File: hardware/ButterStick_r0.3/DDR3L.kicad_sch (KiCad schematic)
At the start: 2 parts, among them U4 MT41K64M16TW-107_J-TR

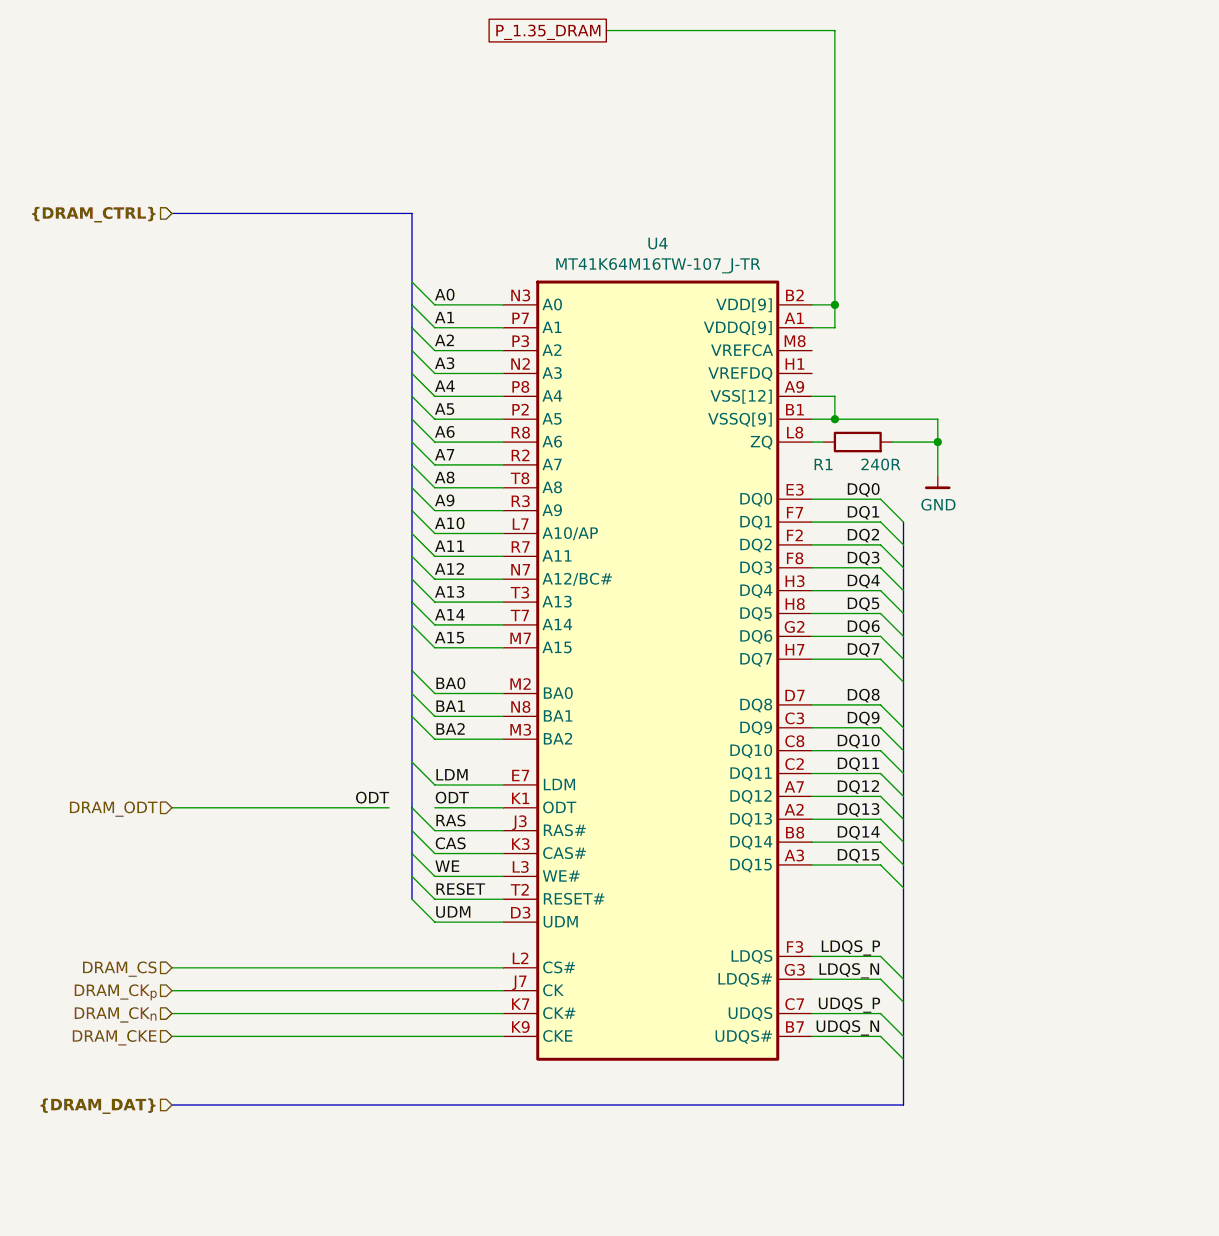
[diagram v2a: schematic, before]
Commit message: hw.r0_3: Inital routing of DDR3 done
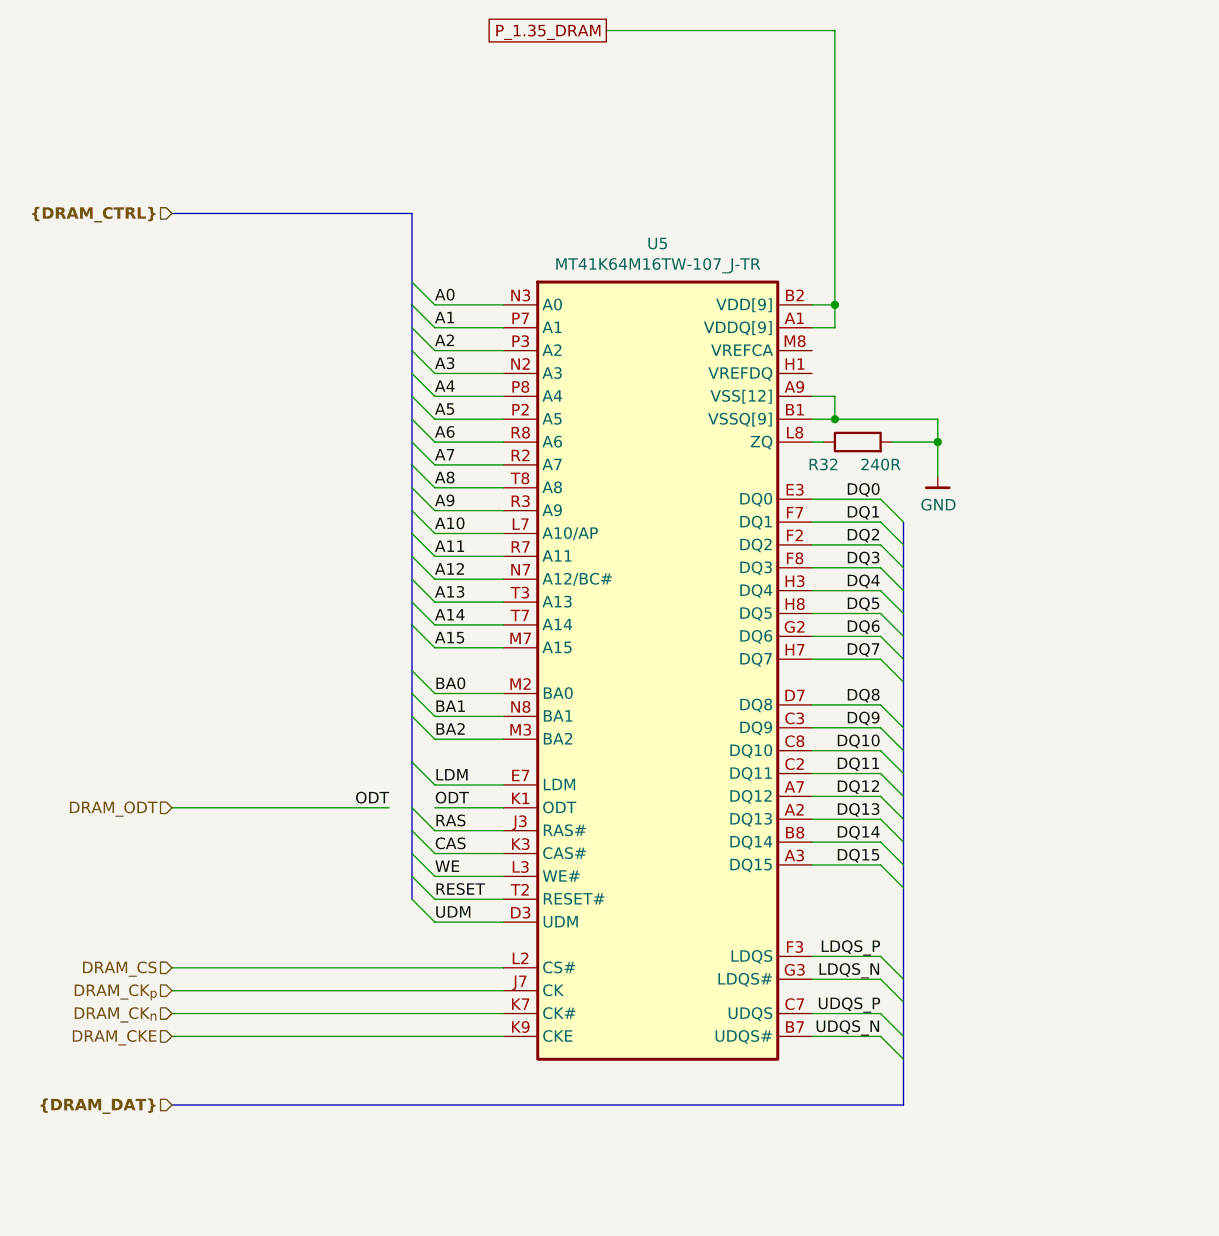
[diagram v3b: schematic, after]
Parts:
- renumbered R1 to R32, U4 to U5
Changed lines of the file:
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@@
 (kicad_sch (version 20200512) (host eeschema "5.99.0-unknown-711fc99~101~ubuntu18.04.1")
-  (page 1 20)
+  (page 14 20)
   (paper "A4")
   (junction (at 157.48 66.04))
@@
   (bus (pts (xy 83.82 154.94) (xy 165.1 154.94)))
   (bus (pts (xy 110.49 55.88) (xy 110.49 66.04)))
-  (bus (pts (xy 110.49 66.04) (xy 110.49 68.58)))
-  (bus (pts (xy 110.49 68.58) (xy 110.49 73.66)))
-  (bus (pts (xy 110.49 73.66) (xy 110.49 78.74)))
+  (bus (pts (xy 110.49 66.04) (xy 110.49 71.12)))
+  (bus (pts (xy 110.49 71.12) (xy 110.49 76.2)))
+  (bus (pts (xy 110.49 76.2) (xy 110.49 78.74)))
   (bus (pts (xy 110.49 78.74) (xy 110.49 83.82)))
   (bus (pts (xy 110.49 83.82) (xy 110.49 88.9)))
-  (bus (pts (xy 110.49 88.9) (xy 110.49 93.98)))
-  (bus (pts (xy 110.49 93.98) (xy 110.49 99.06)))
-  (bus (pts (xy 110.49 99.06) (xy 110.49 106.68)))
-  (bus (pts (xy 110.49 106.68) (xy 110.49 111.76)))
-  (bus (pts (xy 110.49 111.76) (xy 110.49 121.92)))
-  (bus (pts (xy 110.49 121.92) (xy 110.49 127)))
+  (bus (pts (xy 110.49 88.9) (xy 110.49 91.44)))
+  (bus (pts (xy 110.49 91.44) (xy 110.49 96.52)))
+  (bus (pts (xy 110.49 96.52) (xy 110.49 101.6)))
+  (bus (pts (xy 110.49 101.6) (xy 110.49 109.22)))
+  (bus (pts (xy 110.49 109.22) (xy 110.49 116.84)))
+  (bus (pts (xy 110.49 116.84) (xy 110.49 124.46)))
+  (bus (pts (xy 110.49 124.46) (xy 110.49 127)))
   (bus (pts (xy 110.49 127) (xy 110.49 132.08)))
   (bus (pts (xy 165.1 90.17) (xy 165.1 95.25)))
@@
   )
   (symbol (lib_id "Device:R") (at 160.02 81.28 90)
-    (property "Reference" "R1" (id 0) (at 156.21 83.82 90))
+    (property "Reference" "R32" (id 0) (at 156.21 83.82 90))
     (property "Value" "240R" (id 1) (at 162.56 83.82 90))
     (property "Footprint" "" (id 2) (at 160.02 83.058 90)
@@
   )
   (symbol (lib_id "gkl_mem:MT41K512M16TW") (at 137.16 96.52 0)
-    (property "Reference" "U4" (id 0) (at 137.795 59.2582 0))
+    (property "Reference" "U5" (id 0) (at 137.795 59.2582 0))
     (property "Value" "MT41K64M16TW-107_J-TR" (id 1) (at 137.795 61.5442 0))
     (property "Footprint" "Package_BGA:BGA-96_9.0x13.0mm_Layout2x3x16_P0.8mm" (id 2) (at 138.43 58.42 0)

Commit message: hw.r0_3: routed SYZYGY, begin routing RGMII/ULPI
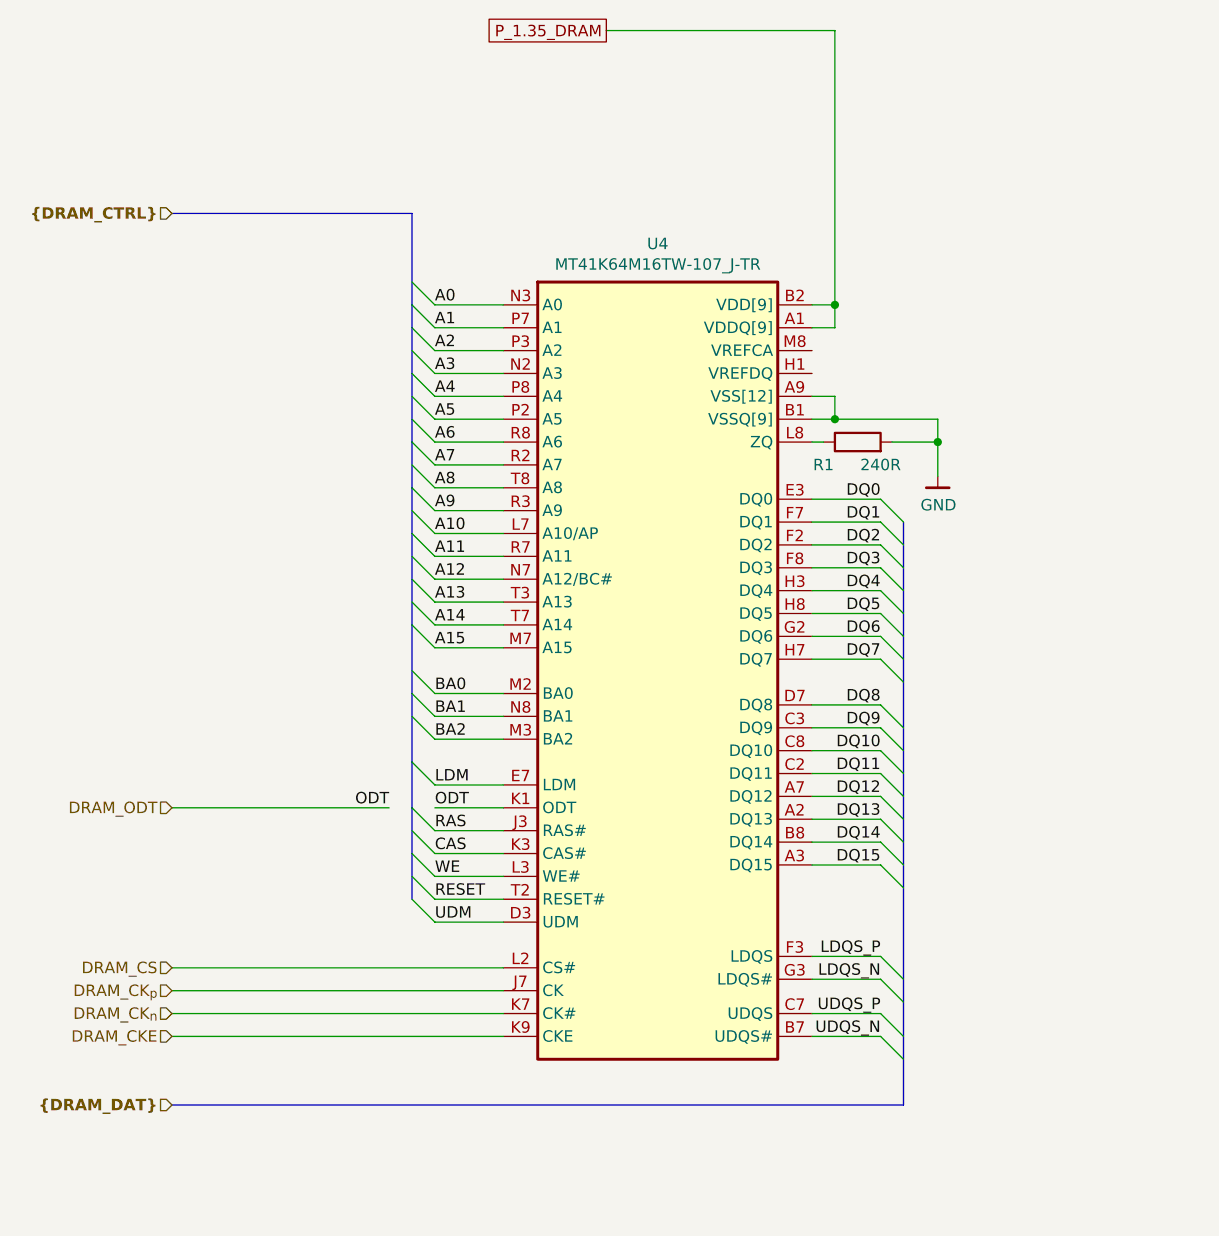
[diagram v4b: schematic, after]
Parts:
- renumbered R32 to R1, U5 to U4
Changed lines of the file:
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@@
 (kicad_sch (version 20200512) (host eeschema "5.99.0-unknown-711fc99~101~ubuntu18.04.1")
-  (page 14 20)
+  (page 1 19)
   (paper "A4")
   (junction (at 157.48 66.04))
@@
   (bus (pts (xy 83.82 154.94) (xy 165.1 154.94)))
   (bus (pts (xy 110.49 55.88) (xy 110.49 66.04)))
-  (bus (pts (xy 110.49 66.04) (xy 110.49 71.12)))
-  (bus (pts (xy 110.49 71.12) (xy 110.49 76.2)))
-  (bus (pts (xy 110.49 76.2) (xy 110.49 78.74)))
-  (bus (pts (xy 110.49 78.74) (xy 110.49 83.82)))
-  (bus (pts (xy 110.49 83.82) (xy 110.49 88.9)))
-  (bus (pts (xy 110.49 88.9) (xy 110.49 91.44)))
+  (bus (pts (xy 110.49 66.04) (xy 110.49 68.58)))
+  (bus (pts (xy 110.49 68.58) (xy 110.49 73.66)))
+  (bus (pts (xy 110.49 73.66) (xy 110.49 78.74)))
+  (bus (pts (xy 110.49 78.74) (xy 110.49 81.28)))
+  (bus (pts (xy 110.49 81.28) (xy 110.49 86.36)))
+  (bus (pts (xy 110.49 86.36) (xy 110.49 91.44)))
   (bus (pts (xy 110.49 91.44) (xy 110.49 96.52)))
   (bus (pts (xy 110.49 96.52) (xy 110.49 101.6)))
   (bus (pts (xy 110.49 101.6) (xy 110.49 109.22)))
   (bus (pts (xy 110.49 109.22) (xy 110.49 116.84)))
-  (bus (pts (xy 110.49 116.84) (xy 110.49 124.46)))
-  (bus (pts (xy 110.49 124.46) (xy 110.49 127)))
+  (bus (pts (xy 110.49 116.84) (xy 110.49 121.92)))
+  (bus (pts (xy 110.49 121.92) (xy 110.49 127)))
   (bus (pts (xy 110.49 127) (xy 110.49 132.08)))
   (bus (pts (xy 165.1 90.17) (xy 165.1 95.25)))
@@
   (bus (pts (xy 165.1 115.57) (xy 165.1 120.65)))
   (bus (pts (xy 165.1 120.65) (xy 165.1 125.73)))
-  (bus (pts (xy 165.1 125.73) (xy 165.1 130.81)))
-  (bus (pts (xy 165.1 130.81) (xy 165.1 143.51)))
+  (bus (pts (xy 165.1 125.73) (xy 165.1 128.27)))
+  (bus (pts (xy 165.1 128.27) (xy 165.1 140.97)))
+  (bus (pts (xy 165.1 140.97) (xy 165.1 143.51)))
   (bus (pts (xy 165.1 143.51) (xy 165.1 149.86)))
   (bus (pts (xy 165.1 149.86) (xy 165.1 154.94)))
@@
   )
   (symbol (lib_id "Device:R") (at 160.02 81.28 90)
-    (property "Reference" "R32" (id 0) (at 156.21 83.82 90))
+    (property "Reference" "R1" (id 0) (at 156.21 83.82 90))
     (property "Value" "240R" (id 1) (at 162.56 83.82 90))
     (property "Footprint" "" (id 2) (at 160.02 83.058 90)
@@
   )
   (symbol (lib_id "gkl_mem:MT41K512M16TW") (at 137.16 96.52 0)
-    (property "Reference" "U5" (id 0) (at 137.795 59.2582 0))
+    (property "Reference" "U4" (id 0) (at 137.795 59.2582 0))
     (property "Value" "MT41K64M16TW-107_J-TR" (id 1) (at 137.795 61.5442 0))
     (property "Footprint" "Package_BGA:BGA-96_9.0x13.0mm_Layout2x3x16_P0.8mm" (id 2) (at 138.43 58.42 0)

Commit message: hw.r0_3: major blocks roughly routed
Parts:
- renumbered R1 to R46, U4 to U7
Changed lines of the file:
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@@
   (bus (pts (xy 110.49 66.04) (xy 110.49 68.58)))
   (bus (pts (xy 110.49 68.58) (xy 110.49 73.66)))
-  (bus (pts (xy 110.49 73.66) (xy 110.49 78.74)))
-  (bus (pts (xy 110.49 78.74) (xy 110.49 81.28)))
+  (bus (pts (xy 110.49 73.66) (xy 110.49 76.2)))
+  (bus (pts (xy 110.49 76.2) (xy 110.49 81.28)))
   (bus (pts (xy 110.49 81.28) (xy 110.49 86.36)))
   (bus (pts (xy 110.49 86.36) (xy 110.49 91.44)))
@@
   (bus (pts (xy 165.1 107.95) (xy 165.1 115.57)))
   (bus (pts (xy 165.1 115.57) (xy 165.1 120.65)))
-  (bus (pts (xy 165.1 120.65) (xy 165.1 125.73)))
-  (bus (pts (xy 165.1 125.73) (xy 165.1 128.27)))
+  (bus (pts (xy 165.1 120.65) (xy 165.1 123.19)))
+  (bus (pts (xy 165.1 123.19) (xy 165.1 128.27)))
   (bus (pts (xy 165.1 128.27) (xy 165.1 140.97)))
   (bus (pts (xy 165.1 140.97) (xy 165.1 143.51)))
@@
   )
   (symbol (lib_id "power:GND") (at 168.91 85.09 0)
-    (property "Reference" "#PWR0224" (id 0) (at 168.91 91.44 0)
+    (property "Reference" "#PWR083" (id 0) (at 168.91 91.44 0)
       (effects (font (size 1.27 1.27)) hide)
     )
@@
   )
   (symbol (lib_id "Device:R") (at 160.02 81.28 90)
-    (property "Reference" "R1" (id 0) (at 156.21 83.82 90))
+    (property "Reference" "R46" (id 0) (at 156.21 83.82 90))
     (property "Value" "240R" (id 1) (at 162.56 83.82 90))
     (property "Footprint" "" (id 2) (at 160.02 83.058 90)
@@
   )
   (symbol (lib_id "gkl_mem:MT41K512M16TW") (at 137.16 96.52 0)
-    (property "Reference" "U4" (id 0) (at 137.795 59.2582 0))
+    (property "Reference" "U7" (id 0) (at 137.795 59.2582 0))
     (property "Value" "MT41K64M16TW-107_J-TR" (id 1) (at 137.795 61.5442 0))
     (property "Footprint" "Package_BGA:BGA-96_9.0x13.0mm_Layout2x3x16_P0.8mm" (id 2) (at 138.43 58.42 0)

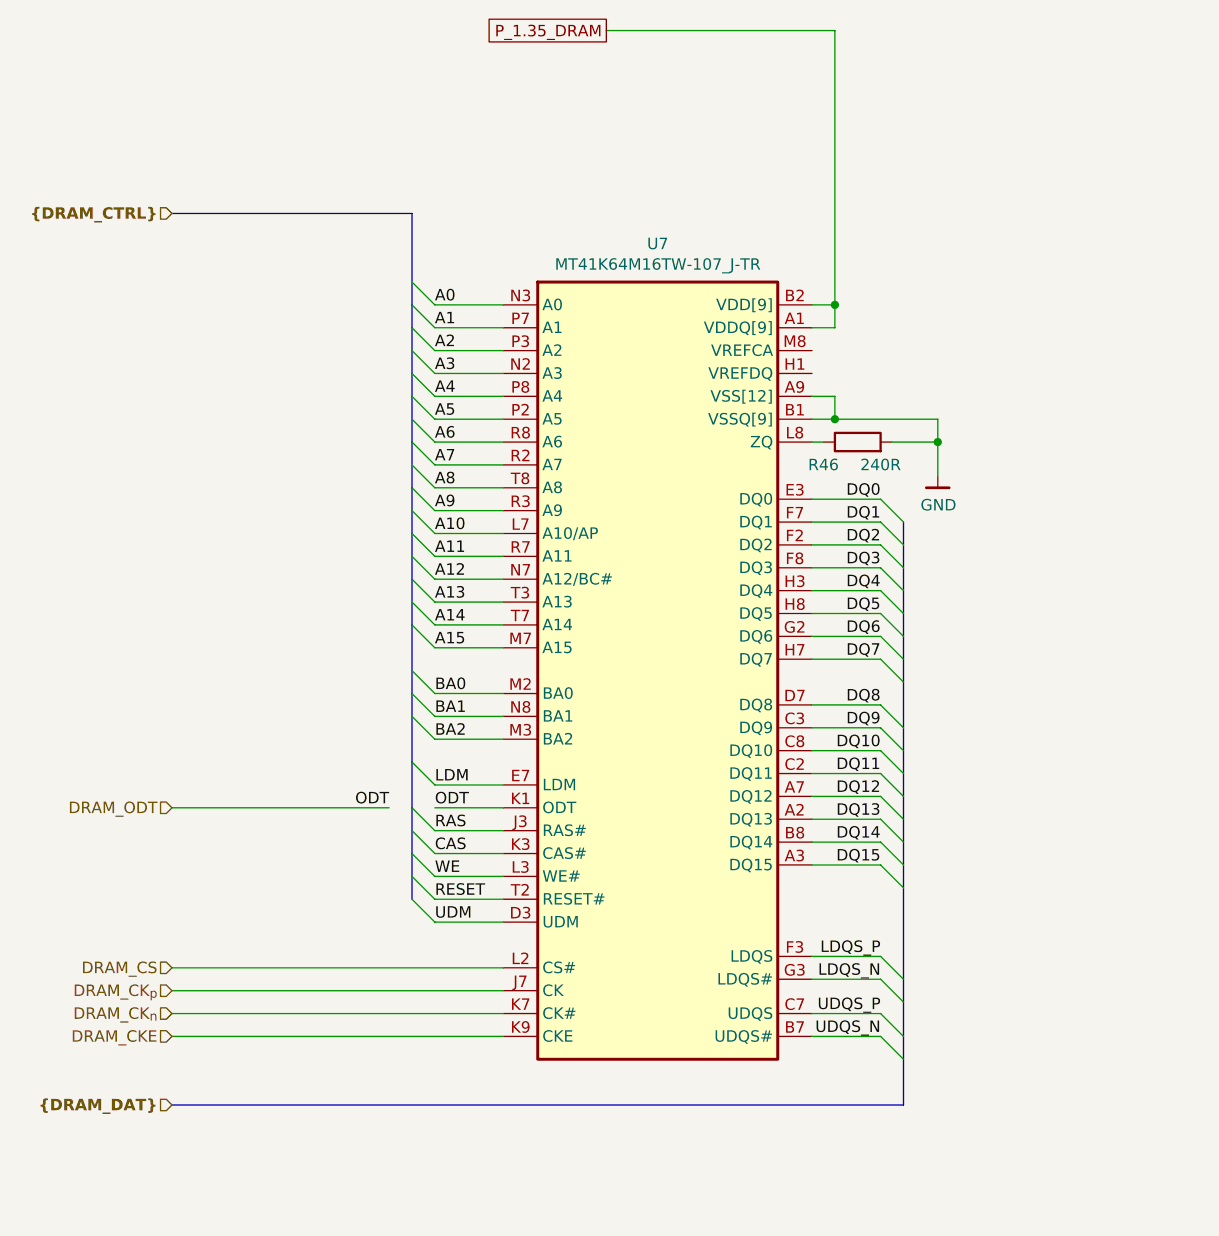
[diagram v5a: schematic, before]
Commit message: hw.r0d3: Length matched all SYZYGY ports
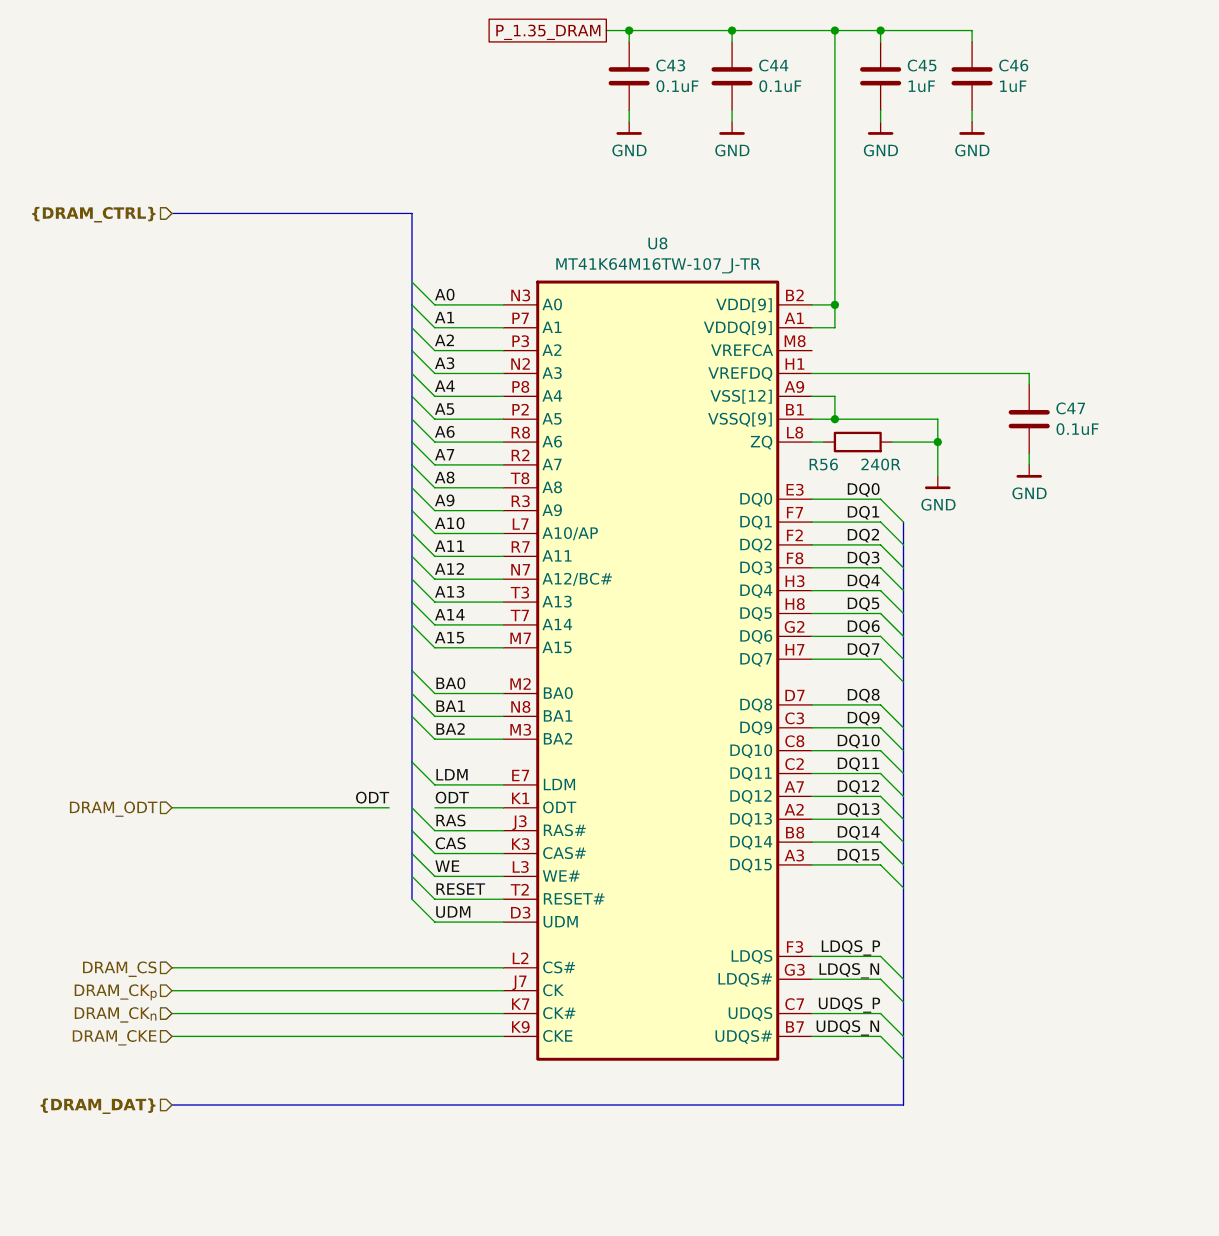
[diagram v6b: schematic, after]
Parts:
- added C43, C44, C47: 0.1uF, Capacitor_SMD:C_0402_1005Metric, symbol Device:C
- added C45, C46: 1uF, Capacitor_SMD:C_0402_1005Metric, symbol Device:C
- R56: renamed from R46; footprint (none) -> Resistor_SMD:R_0402_1005Metric
- renumbered U7 to U8
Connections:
- net GND: now also C43.2, C44.2, C45.2, C46.2, C47.2
- net P_1.35_DRAM: now also C43.1, C44.1, C45.1, C46.1
- net at U8.H1 (VREFDQ): now also C47.1
